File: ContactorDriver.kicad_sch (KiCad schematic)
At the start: 32 parts, among them J1 PowerConn, J2 DashboardConnA, J3 ContactorAConn, J4 FanConn1, J5 FanConn2, J6 DashboardConnB, J7 ContactorBConn, J8 FanConn3, Q1 IRLML0030TRPbF, Q2 IRLML0030TRPbF, Q3 IRLML0030TRPbF

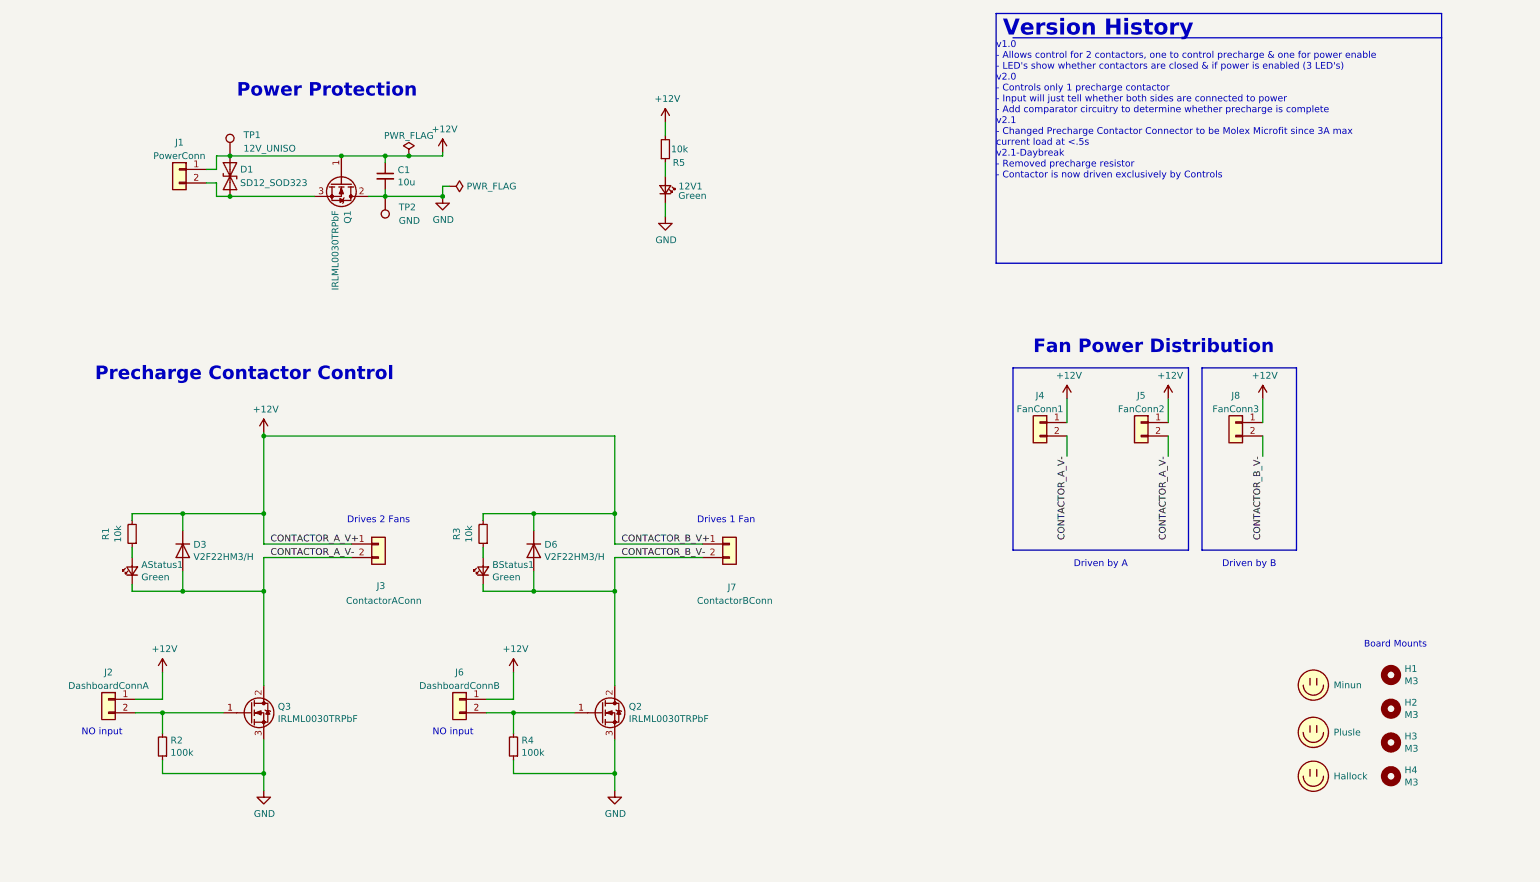
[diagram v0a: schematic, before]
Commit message: Changed out schottky diodes + updated changelog
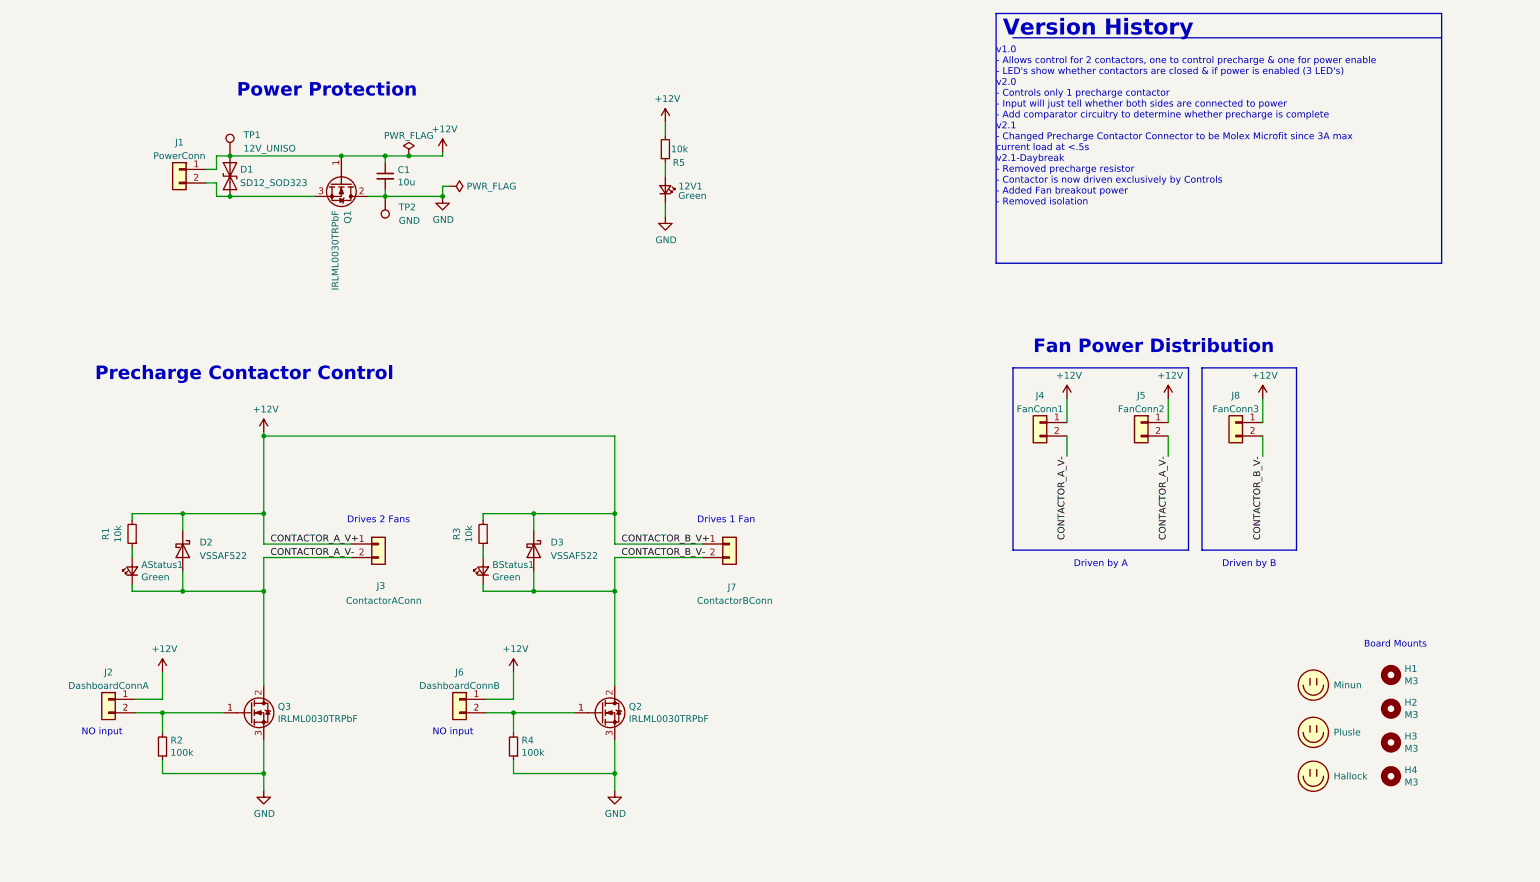
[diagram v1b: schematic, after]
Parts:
- removed D3, D6: V2F22HM3/H, UTSVT_Passive:V2F22HM, symbol Device:D
- added D2, D3: VSSAF522, UTSVT_Passive:DO-221AC, symbol Device:D_Schottky
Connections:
- net +12V: now also D2.1 (K), D3.1 (K)
- net CONTACTOR_A_V-: now also D2.2 (A)
- net CONTACTOR_B_V-: now also D3.2 (A)
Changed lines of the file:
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@@
 		)
 	)
-	(text "v1.0\n- Allows control for 2 contactors, one to control precharge & one for power enable\n- LED's show whether contactors are closed & if power is enabled (3 LED's)\nv2.0\n- Controls only 1 precharge contactor\n- Input will just tell whether both sides are connected to power\n- Add comparator circuitry to determine whether precharge is complete\nv2.1\n- Changed Precharge Contactor Connector to be Molex Microfit since 3A max \ncurrent load at <.5s\nv2.1-Daybreak\n- Removed precharge resistor\n- Contactor is now driven exclusively by Controls"
-		(exclude_from_sim no)
-		(at 198.755 45.085 0)
+	(text "v1.0\n- Allows control for 2 contactors, one to control precharge & one for power enable\n- LED's show whether contactors are closed & if power is enabled (3 LED's)\nv2.0\n- Controls only 1 precharge contactor\n- Input will just tell whether both sides are connected to power\n- Add comparator circuitry to determine whether precharge is complete\nv2.1\n- Changed Precharge Contactor Connector to be Molex Microfit since 3A max \ncurrent load at <.5s\nv2.1-Daybreak\n- Removed precharge resistor\n- Contactor is now driven exclusively by Controls\n- Added Fan breakout power\n- Removed isolation"
+		(exclude_from_sim no)
+		(at 198.755 50.165 0)
 		(effects
 			(font
@@
 	)
 	(symbol
+		(lib_id "Device:D_Schottky")
+		(at 111.76 114.935 270)
+		(unit 1)
+		(exclude_from_sim no)
+		(in_bom yes)
+		(on_board yes)
+		(dnp no)
+		(fields_autoplaced yes)
+		(property "Reference" "D3"
+			(at 114.935 113.3474 90)
+			(effects
+				(font
+					(size 1.27 1.27)
+				)
+				(justify left)
+			)
+		)
+		(property "Value" "VSSAF522"
+			(at 114.935 115.8874 90)
+			(effects
+				(font
+					(size 1.27 1.27)
+				)
+				(justify left)
+			)
+		)
+		(property "Footprint" "UTSVT_Passive:DO-221AC"
+			(at 111.76 114.935 0)
+			(effects
+				(font
+					(size 1.27 1.27)
+				)
+				(hide yes)
+			)
+		)
+		(property "Datasheet" "https://www.vishay.com/docs/87453/vssaf522.pdf"
+			(at 111.76 114.935 0)
+			(effects
+				(font
+					(size 1.27 1.27)
+				)
+				(hide yes)
+			)
+		)
+		(property "Description" "200V 2A Trench MOS Barrier Schottky Diode"
+			(at 111.76 114.935 0)
+			(effects
+				(font
+					(size 1.27 1.27)
+				)
+				(hide yes)
+			)
+		)
+		(pin "1"
+		)
+		(pin "2"
+		)
+		(instances
+			(project "ContactorDriver"
+				(path "/aaa5c8ef-bb12-4c4a-bd2b-ddbca3d09ae8"
+					(reference "D3")
+					(unit 1)
+				)
+			)
+		)
+	)
+	(symbol
 		(lib_id "power:+12V")
 		(at 231.14 86.36 0)
@@
 	)
 	(symbol
-		(lib_id "Device:D")
-		(at 111.76 114.935 270)
-		(unit 1)
-		(exclude_from_sim no)
-		(in_bom yes)
-		(on_board yes)
-		(dnp no)
-		(property "Reference" "D6"
-			(at 113.7666 113.7666 90)
-			(effects
-				(font
-					(size 1.27 1.27)
-				)
-				(justify left)
-			)
-		)
-		(property "Value" "V2F22HM3/H"
-			(at 113.7666 116.078 90)
-			(effects
-				(font
-					(size 1.27 1.27)
-				)
-				(justify left)
-			)
-		)
-		(property "Footprint" "UTSVT_Passive:V2F22HM"
-			(at 111.76 114.935 0)
-			(effects
-				(font
-					(size 1.27 1.27)
-				)
-				(hide yes)
-			)
-		)
-		(property "Datasheet" "https://www.mouser.com/datasheet/2/427/v2f22-1767661.pdf"
-			(at 111.76 114.935 0)
-			(effects
-				(font
-					(size 1.27 1.27)
-				)
-				(hide yes)
-			)
-		)
-		(property "Description" ""
-			(at 111.76 114.935 0)
-			(effects
-				(font
-					(size 1.27 1.27)
-				)
-				(hide yes)
-			)
-		)
-		(property "Mouser" "https://www.mouser.com/ProductDetail/Vishay-Semiconductors/V2F22HM3-H?qs=BJlw7L4Cy78MY7ajCA04cw%3D%3D"
-			(at 111.76 114.935 90)
-			(effects
-				(font
-					(size 1.27 1.27)
-				)
-				(hide yes)
-			)
-		)
-		(property "P/N" "V2F22"
-			(at 111.76 114.935 0)
-			(effects
-				(font
-					(size 1.27 1.27)
-				)
-				(hide yes)
-			)
-		)
-		(pin "1"
-		)
-		(pin "2"
-		)
-		(instances
-			(project "ContactorDriver"
-				(path "/aaa5c8ef-bb12-4c4a-bd2b-ddbca3d09ae8"
-					(reference "D6")
-					(unit 1)
-				)
-			)
-		)
-	)
-	(symbol
 		(lib_id "Device:R_Small")
 		(at 41.91 151.765 180)
@@
 	)
 	(symbol
+		(lib_id "Device:D_Schottky")
+		(at 45.72 114.935 270)
+		(unit 1)
+		(exclude_from_sim no)
+		(in_bom yes)
+		(on_board yes)
+		(dnp no)
+		(fields_autoplaced yes)
+		(property "Reference" "D2"
+			(at 48.895 113.3474 90)
+			(effects
+				(font
+					(size 1.27 1.27)
+				)
+				(justify left)
+			)
+		)
+		(property "Value" "VSSAF522"
+			(at 48.895 115.8874 90)
+			(effects
+				(font
+					(size 1.27 1.27)
+				)
+				(justify left)
+			)
+		)
+		(property "Footprint" "UTSVT_Passive:DO-221AC"
+			(at 45.72 114.935 0)
+			(effects
+				(font
+					(size 1.27 1.27)
+				)
+				(hide yes)
+			)
+		)
+		(property "Datasheet" "https://www.vishay.com/docs/87453/vssaf522.pdf"
+			(at 45.72 114.935 0)
+			(effects
+				(font
+					(size 1.27 1.27)
+				)
+				(hide yes)
+			)
+		)
+		(property "Description" "200V 2A Trench MOS Barrier Schottky Diode"
+			(at 45.72 114.935 0)
+			(effects
+				(font
+					(size 1.27 1.27)
+				)
+				(hide yes)
+			)
+		)
+		(pin "1"
+		)
+		(pin "2"
+		)
+		(instances
+			(project "ContactorDriver"
+				(path "/aaa5c8ef-bb12-4c4a-bd2b-ddbca3d09ae8"
+					(reference "D2")
+					(unit 1)
+				)
+			)
+		)
+	)
+	(symbol
 		(lib_id "Diode:SD12_SOD323")
 		(at 54.61 44.45 90)
@@
 					(unit 1)
 				)
-			)
-		)
-	)
-	(symbol
-		(lib_id "Device:D")
-		(at 45.72 114.935 270)
-		(unit 1)
-		(exclude_from_sim no)
-		(in_bom yes)
-		(on_board yes)
-		(dnp no)
-		(property "Reference" "D3"
-			(at 47.7266 113.7666 90)
-			(effects
-				(font
-					(size 1.27 1.27)
-				)
-				(justify left)
-			)
-		)
-		(property "Value" "V2F22HM3/H"
-			(at 47.7266 116.078 90)
-			(effects
-				(font
-					(size 1.27 1.27)
-				)
-				(justify left)
-			)
-		)
-		(property "Footprint" "UTSVT_Passive:V2F22HM"
-			(at 45.72 114.935 0)
-			(effects
-				(font
-					(size 1.27 1.27)
-				)
-				(hide yes)
-			)
-		)
-		(property "Datasheet" "https://www.mouser.com/datasheet/2/427/v2f22-1767661.pdf"
-			(at 45.72 114.935 0)
-			(effects
-				(font
-					(size 1.27 1.27)
-				)
-				(hide yes)
-			)
-		)
-		(property "Description" ""
-			(at 45.72 114.935 0)
-			(effects
-				(font
-					(size 1.27 1.27)
-				)
-				(hide yes)
-			)
-		)
-		(property "Mouser" "https://www.mouser.com/ProductDetail/Vishay-Semiconductors/V2F22HM3-H?qs=BJlw7L4Cy78MY7ajCA04cw%3D%3D"
-			(at 45.72 114.935 90)
-			(effects
-				(font
-					(size 1.27 1.27)
-				)
-				(hide yes)
-			)
-		)
-		(property "P/N" "V2F22"
-			(at 45.72 114.935 0)
-			(effects
-				(font
-					(size 1.27 1.27)
-				)
-				(hide yes)
-			)
-		)
-		(pin "1"
-		)
-		(pin "2"
-		)
-		(instances
-			(project "ContactorDriver"
-				(path "/aaa5c8ef-bb12-4c4a-bd2b-ddbca3d09ae8"
-					(reference "D3")
-					(unit 1)
-				)
-			)
-			(project "BPS-Leader"
-				(path "/c248b171-df31-4e8a-afb6-607fa2df334b/00000000-0000-0000-0000-00005c38c674"
-					(reference "D12")
-					(unit 1)
-				)

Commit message: Added one more contactor, and another fan conn
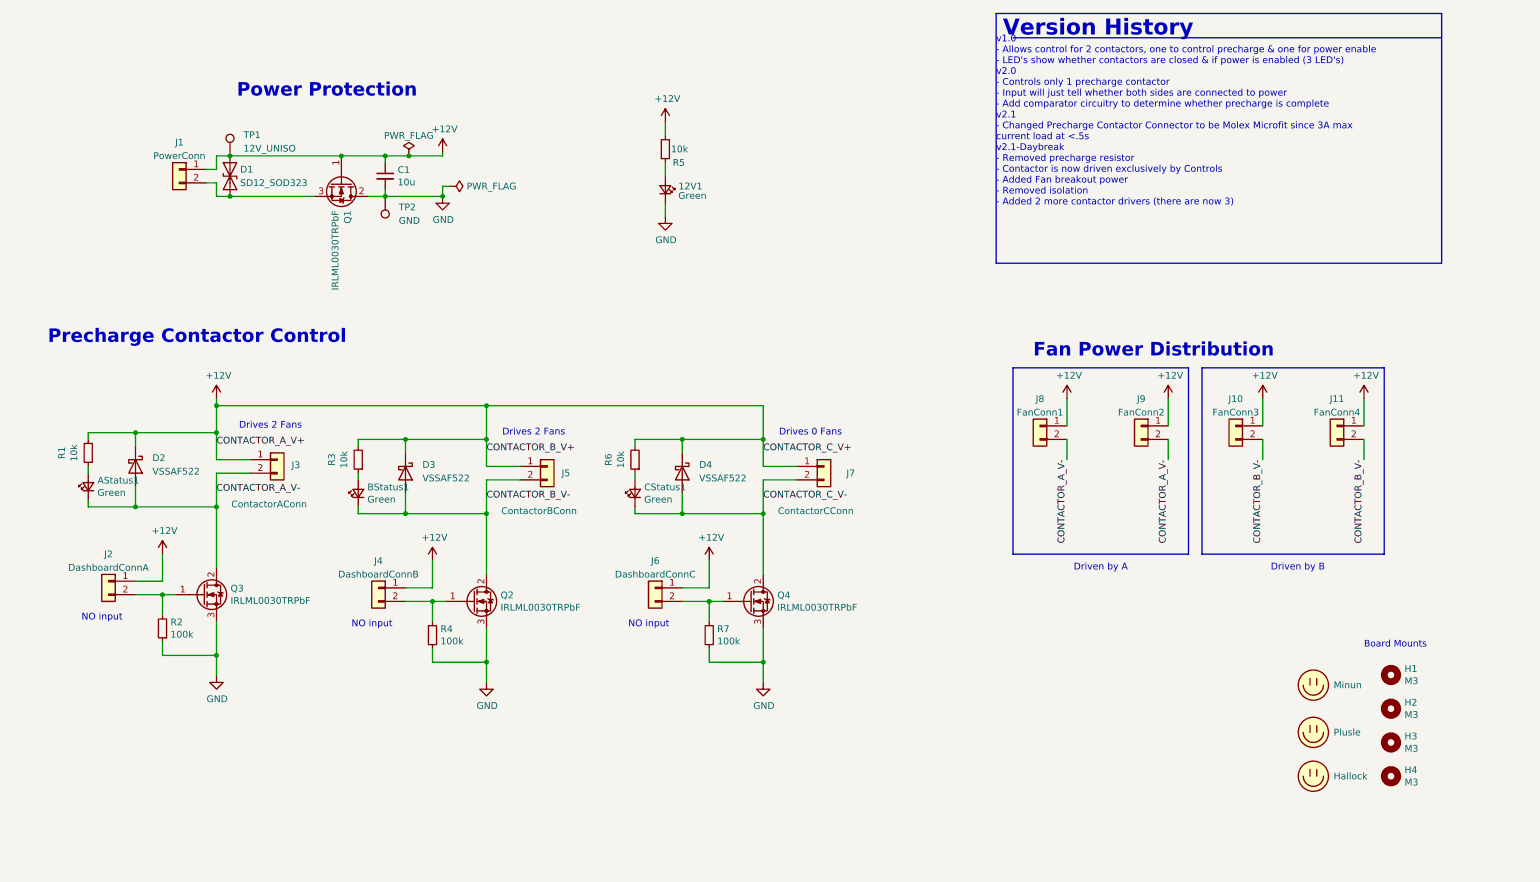
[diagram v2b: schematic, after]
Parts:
- added CStatus1: Green, LED_SMD:LED_0805_2012Metric_Pad1.15x1.40mm_HandSolder, symbol Device:LED_Small
- added D4: VSSAF522, UTSVT_Passive:DO-221AC, symbol Device:D_Schottky
- added J11: FanConn4, Connector_Molex:Molex_Micro-Fit_3.0_43650-0215_1x02_P3.00mm_Vertical, symbol Connector_Generic:Conn_01x02
- added J6: DashboardConnC, Connector_Molex:Molex_Micro-Fit_3.0_43650-0215_1x02_P3.00mm_Vertical, symbol Connector_Generic:Conn_01x02
- added J7: ContactorCConn, Connector_Molex:Molex_Micro-Fit_3.0_43650-0215_1x02_P3.00mm_Vertical, symbol Connector_Generic:Conn_01x02
- added Q4: IRLML0030TRPbF, Package_TO_SOT_SMD:SOT-23, symbol Device:Q_NMOS_GDS
- added R6: 10k, Resistor_SMD:R_0805_2012Metric, symbol Device:R_Small
- added R7: 100k, Resistor_SMD:R_0805_2012Metric_Pad1.20x1.40mm_HandSolder, symbol Device:R_Small
- renumbered J8 to J10, J6 to J4, J7 to J5, J4 to J8, J5 to J9
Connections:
- net +12V: now also D4.1 (K), J11.1 (Pin_1), J6.1 (Pin_1), J7.1 (Pin_1), R6.2
- net CONTACTOR_B_V-: now also J11.2 (Pin_2)
- net GND: now also Q4.3 (S), R7.1
- new net: J6.2 (Pin_2), Q4.1 (G), R7.2
- new net: CStatus1.2 (A), R6.1
- new net CONTACTOR_C_V-: CStatus1.1 (K), D4.2 (A), J7.2 (Pin_2), Q4.2 (D)
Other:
- note added: "Drives 0 Fans"
- note removed: "Drives 1 Fan"
- moved on the sheet: AStatus1, BStatus1, D2, D3, J10, J2, J3, J4, J5, J8, J9, Q2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

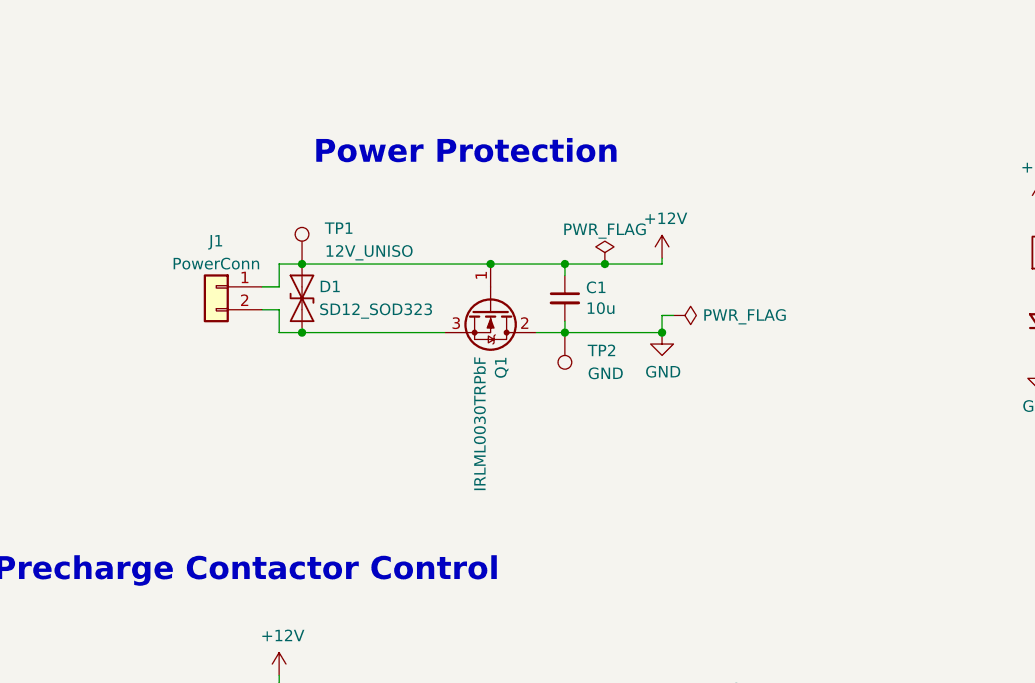
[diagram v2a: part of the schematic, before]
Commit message: Fixed reverse polarity protection circuitry
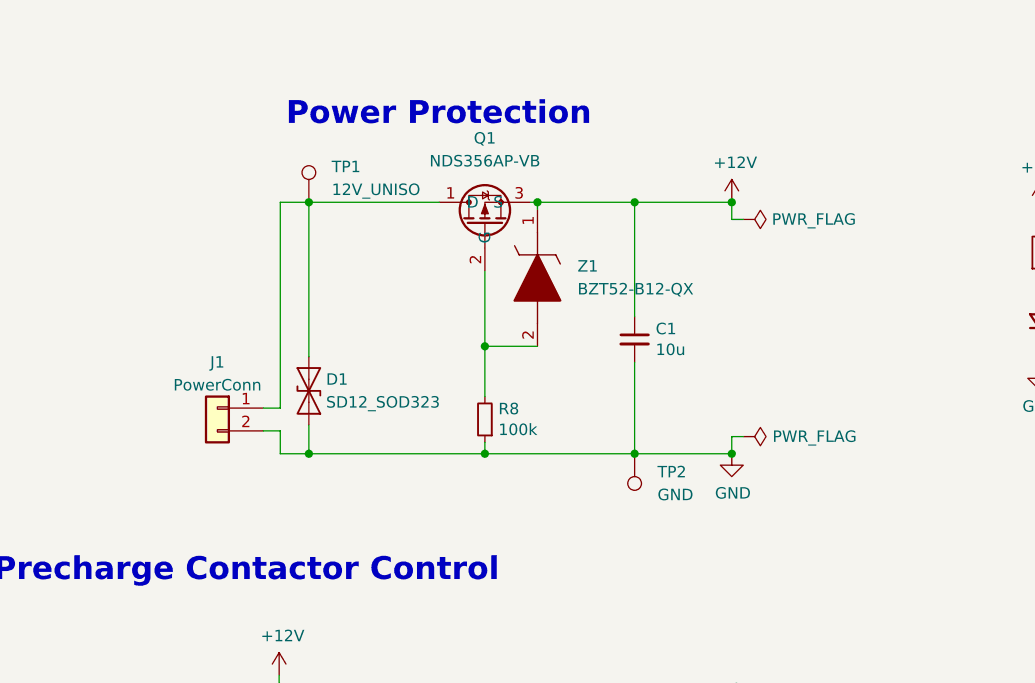
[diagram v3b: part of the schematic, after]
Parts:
- removed Q1: IRLML0030TRPbF, Package_TO_SOT_SMD:SOT-23, symbol Device:Q_NMOS_GDS
- added Q1: NDS356AP-VB, Package_TO_SOT_SMD:SOT-23, symbol utsvt-chips:NDS356AP-VB
- added R8: 100k, Resistor_SMD:R_0805_2012Metric_Pad1.20x1.40mm_HandSolder, symbol Device:R_Small
- added Z1: BZT52-B12-QX, BZT52B12QX, symbol BZT52-B12-QX:BZT52-B12-QX
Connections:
- net +12V: now also Q1.3 (S), Z1.1; no longer D1.2 (A2), J1.1 (Pin_1), TP1.1
- net GND: now also D1.1 (A1), J1.2 (Pin_2), R8.1
- new net: D1.2 (A2), J1.1 (Pin_1), Q1.1 (D), TP1.1
- new net: Q1.2 (G), R8.2, Z1.2
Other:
- moved on the sheet: C1, D1, J1, TP1, TP2
